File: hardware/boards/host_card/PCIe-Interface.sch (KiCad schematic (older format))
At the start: 10 parts, among them U1 ECP5UM5G-381caBGA, U7 SI5330B

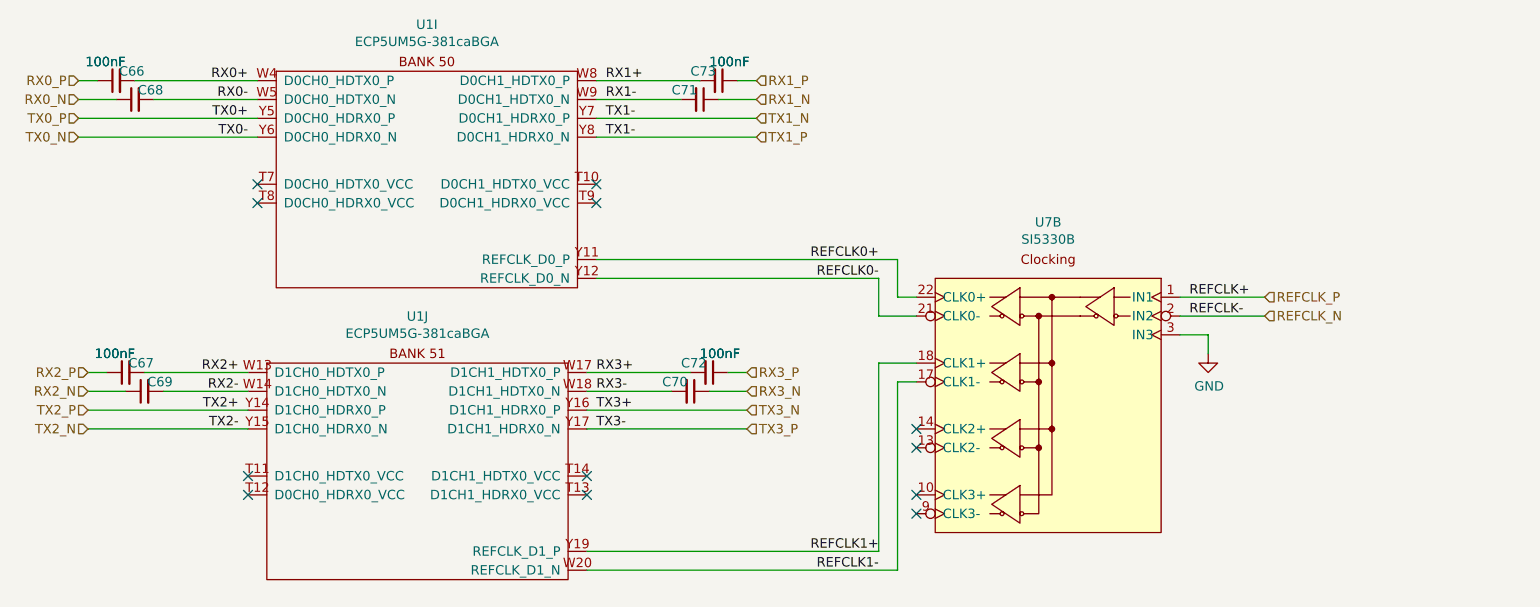
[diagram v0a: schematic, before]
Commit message: Routed the PCIe TX and RX lines + wiggles, activly routing the clock
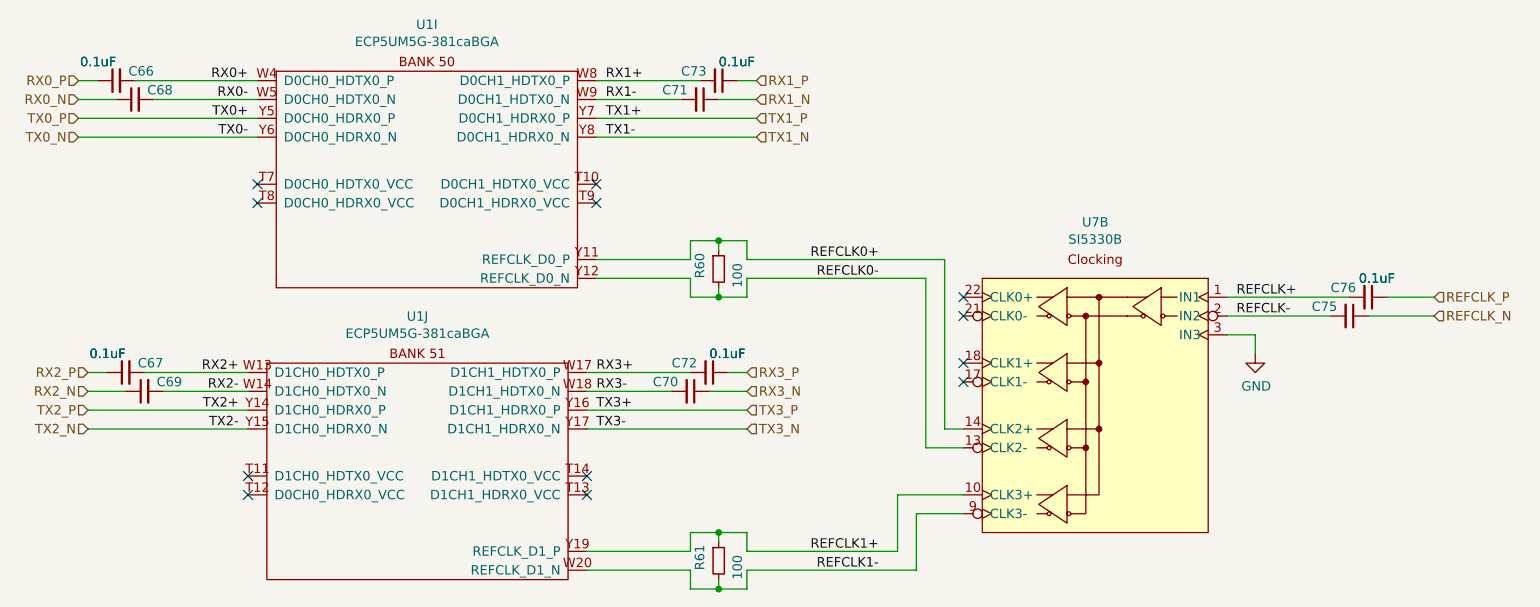
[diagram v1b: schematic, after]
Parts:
- added C75, C76: 0.1uF, Capacitor_SMD:C_0402_1005Metric, symbol Device:C_Small
- added R60, R61: 100, Resistor_SMD:R_0402_1005Metric, symbol Device:R_Small
- C66, C67, C68, C69, C70, C71, C72, C73: value 100nF -> 0.1uF
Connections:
- net REFCLK0+: now also U7.14 (CLK2+), R60.1; no longer U7.22 (CLK0+)
- net REFCLK0-: now also U7.13 (CLK2-), R60.2; no longer U7.21 (CLK0-)
- net REFCLK1+: now also U7.10 (CLK3+), R61.1; no longer U7.18 (CLK1+)
- net REFCLK1-: now also U7.9 (CLK3-), R61.2; no longer U7.17 (CLK1-)
- net REFCLK_N: now also C75.1; no longer U7.2 (IN2)
- net REFCLK_P: now also C76.1; no longer U7.1 (IN1)
- net TX1_N: no longer U1.Y7 (D0CH1_HDRX0_P)
- net TX3_N: now also U1.Y17 (D1CH1_HDRX0_N); no longer U1.Y16 (D1CH1_HDRX0_P)
- net TX3_P: now also U1.Y16 (D1CH1_HDRX0_P); no longer U1.Y17 (D1CH1_HDRX0_N)
- new net REFCLK+: C76.2, U7.1 (IN1)
- new net REFCLK-: C75.2, U7.2 (IN2)
- new net TX1_P: U1.Y7 (D0CH1_HDRX0_P)
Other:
- moved on the sheet: U7B
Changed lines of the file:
@@
 Comment4 ""
 $EndDescr
-Text HLabel 10500 3400 2    50   Input ~ 0
+Text HLabel 11400 3400 2    50   Input ~ 0
 REFCLK_P
-Text HLabel 10500 3500 2    50   Input ~ 0
+Text HLabel 11400 3500 2    50   Input ~ 0
 REFCLK_N
 Text HLabel 4200 2450 0    50   Input ~ 0
@@
 Text HLabel 4200 2550 0    50   Input ~ 0
 TX0_N
+Text HLabel 7800 2450 2    50   Input ~ 0
+TX1_P
 Text HLabel 7800 2550 2    50   Input ~ 0
-TX1_P
-Text HLabel 7800 2450 2    50   Input ~ 0
 TX1_N
 Text HLabel 4250 4000 0    50   Input ~ 0
@@
 Text HLabel 4250 4100 0    50   Input ~ 0
 TX2_N
+Text HLabel 7750 4000 2    50   Input ~ 0
+TX3_P
 Text HLabel 7750 4100 2    50   Input ~ 0
-TX3_P
-Text HLabel 7750 4000 2    50   Input ~ 0
 TX3_N
 Text HLabel 4200 2250 0    50   Input ~ 0
@@
 L lethalbit:SI5330B U7
 U 2 1 5F1A1842
-P 9350 3400
-F 0 "U7" H 9350 3798 50  0000 C CNN
-F 1 "SI5330B" H 9350 3707 50  0000 C CNN
-F 2 "Package_DFN_QFN:VQFN-24-1EP_4x4mm_P0.5mm_EP2.45x2.45mm" H 9350 3700 50  0001 C CNN
-F 3 "https://www.silabs.com/documents/public/data-sheets/Si5330.pdf" H 9350 3700 50  0001 C CNN
-F 4 "Silicon Labs" H 9350 3400 50  0001 C CNN "MFR"
-F 5 "SI5330B-B00205-GM" H 9350 3400 50  0001 C CNN "MPN"
-	2    9350 3400
+P 9600 3400
+F 0 "U7" H 9600 3798 50  0000 C CNN
+F 1 "SI5330B" H 9600 3707 50  0000 C CNN
+F 2 "Package_DFN_QFN:VQFN-24-1EP_4x4mm_P0.5mm_EP2.45x2.45mm" H 9600 3700 50  0001 C CNN
+F 3 "https://www.silabs.com/documents/public/data-sheets/Si5330.pdf" H 9600 3700 50  0001 C CNN
+F 4 "Silicon Labs" H 9600 3400 50  0001 C CNN "MFR"
+F 5 "SI5330B-B00205-GM" H 9600 3400 50  0001 C CNN "MPN"
+	2    9600 3400
 	-1   0    0    -1
 $EndComp
 Wire Wire Line
-	10050 3400 10500 3400
-Wire Wire Line
-	10050 3500 10500 3500
+	10300 3400 10950 3400
+Wire Wire Line
+	10300 3500 10850 3500
 $Comp
 L power:GND #PWR0142
 U 1 1 5F1DBF37
-P 10200 3700
-F 0 "#PWR0142" H 10200 3450 50  0001 C CNN
-F 1 "GND" H 10205 3527 50  0000 C CNN
-F 2 "" H 10200 3700 50  0001 C CNN
-F 3 "" H 10200 3700 50  0001 C CNN
-	1    10200 3700
+P 10450 3700
+F 0 "#PWR0142" H 10450 3450 50  0001 C CNN
+F 1 "GND" H 10455 3527 50  0000 C CNN
+F 2 "" H 10450 3700 50  0001 C CNN
+F 3 "" H 10450 3700 50  0001 C CNN
+	1    10450 3700
 	1    0    0    -1
 $EndComp
 Wire Wire Line
-	10050 3600 10200 3600
-Wire Wire Line
-	10200 3600 10200 3700
-NoConn ~ 8650 4100
-NoConn ~ 8650 4200
-NoConn ~ 8650 4450
-NoConn ~ 8650 4550
-Wire Wire Line
-	8650 3400 8550 3400
-Wire Wire Line
-	8550 3400 8550 3200
-Wire Wire Line
-	8550 3200 6950 3200
-Wire Wire Line
-	8650 3500 8450 3500
-Wire Wire Line
-	8450 3500 8450 3300
-Wire Wire Line
-	8450 3300 6950 3300
-Wire Wire Line
-	6900 4750 8450 4750
-Wire Wire Line
-	8450 4750 8450 3750
-Wire Wire Line
-	8450 3750 8650 3750
-Wire Wire Line
-	6900 4850 8550 4850
-Wire Wire Line
-	8550 4850 8550 3850
-Wire Wire Line
-	8550 3850 8650 3850
+	10300 3600 10450 3600
+Wire Wire Line
+	10450 3600 10450 3700
 Text Label 8450 3200 2    50   ~ 0
 REFCLK0+
@@
 AR Path="/5EF66188/5F46D592" Ref="C?"  Part="1"
 AR Path="/5ED4B101/5F46D592" Ref="C66"  Part="1"
-F 0 "C66" V 4450 2100 50  0000 L CNN
-F 1 "100nF" V 4500 2200 50  0000 L CNN
+F 0 "C66" V 4450 2050 50  0000 L CNN
+F 1 "0.1uF" V 4500 2250 50  0000 L CNN
 F 2 "Capacitor_SMD:C_0402_1005Metric" H 4400 2250 50  0001 C CNN
 F 3 "~" H 4400 2250 50  0001 C CNN
@@
 AR Path="/5EF66188/5F4C2DB2" Ref="C?"  Part="1"
 AR Path="/5ED4B101/5F4C2DB2" Ref="C68"  Part="1"
-F 0 "C68" V 4550 2200 50  0000 L CNN
-F 1 "100nF" V 4700 2400 50  0000 L CNN
+F 0 "C68" V 4550 2150 50  0000 L CNN
+F 1 "0.1uF" V 4700 2450 50  0000 L CNN
 F 2 "Capacitor_SMD:C_0402_1005Metric" H 4500 2350 50  0001 C CNN
 F 3 "~" H 4500 2350 50  0001 C CNN
@@
 AR Path="/5EF66188/5F524C27" Ref="C?"  Part="1"
 AR Path="/5ED4B101/5F524C27" Ref="C73"  Part="1"
-F 0 "C73" V 7650 2100 50  0000 L CNN
-F 1 "100nF" V 7700 2200 50  0000 L CNN
+F 0 "C73" V 7650 2050 50  0000 L CNN
+F 1 "0.1uF" V 7700 2250 50  0000 L CNN
 F 2 "Capacitor_SMD:C_0402_1005Metric" H 7600 2250 50  0001 C CNN
 F 3 "~" H 7600 2250 50  0001 C CNN
@@
 AR Path="/5EF66188/5F524C2F" Ref="C?"  Part="1"
 AR Path="/5ED4B101/5F524C2F" Ref="C71"  Part="1"
-F 0 "C71" V 7550 2200 50  0000 L CNN
-F 1 "100nF" V 7700 2400 50  0000 L CNN
+F 0 "C71" V 7550 2150 50  0000 L CNN
+F 1 "0.1uF" V 7700 2450 50  0000 L CNN
 F 2 "Capacitor_SMD:C_0402_1005Metric" H 7500 2350 50  0001 C CNN
 F 3 "~" H 7500 2350 50  0001 C CNN
@@
 AR Path="/5EF66188/5F527EEF" Ref="C?"  Part="1"
 AR Path="/5ED4B101/5F527EEF" Ref="C67"  Part="1"
-F 0 "C67" V 4500 3650 50  0000 L CNN
-F 1 "100nF" V 4550 3750 50  0000 L CNN
+F 0 "C67" V 4500 3600 50  0000 L CNN
+F 1 "0.1uF" V 4550 3800 50  0000 L CNN
 F 2 "Capacitor_SMD:C_0402_1005Metric" H 4450 3800 50  0001 C CNN
 F 3 "~" H 4450 3800 50  0001 C CNN
@@
 AR Path="/5EF66188/5F527EF7" Ref="C?"  Part="1"
 AR Path="/5ED4B101/5F527EF7" Ref="C69"  Part="1"
-F 0 "C69" V 4600 3750 50  0000 L CNN
-F 1 "100nF" V 4750 3950 50  0000 L CNN
+F 0 "C69" V 4600 3700 50  0000 L CNN
+F 1 "0.1uF" V 4750 4000 50  0000 L CNN
 F 2 "Capacitor_SMD:C_0402_1005Metric" H 4550 3900 50  0001 C CNN
 F 3 "~" H 4550 3900 50  0001 C CNN
@@
 AR Path="/5EF66188/5F52A5F2" Ref="C?"  Part="1"
 AR Path="/5ED4B101/5F52A5F2" Ref="C72"  Part="1"
-F 0 "C72" V 7600 3650 50  0000 L CNN
-F 1 "100nF" V 7650 3750 50  0000 L CNN
+F 0 "C72" V 7600 3600 50  0000 L CNN
+F 1 "0.1uF" V 7650 3800 50  0000 L CNN
 F 2 "Capacitor_SMD:C_0402_1005Metric" H 7550 3800 50  0001 C CNN
 F 3 "~" H 7550 3800 50  0001 C CNN
@@
 AR Path="/5EF66188/5F52A5FA" Ref="C?"  Part="1"
 AR Path="/5ED4B101/5F52A5FA" Ref="C70"  Part="1"
-F 0 "C70" V 7500 3750 50  0000 L CNN
-F 1 "100nF" V 7650 3950 50  0000 L CNN
+F 0 "C70" V 7500 3700 50  0000 L CNN
+F 1 "0.1uF" V 7650 4000 50  0000 L CNN
 F 2 "Capacitor_SMD:C_0402_1005Metric" H 7450 3900 50  0001 C CNN
 F 3 "~" H 7450 3900 50  0001 C CNN
@@
 Text Label 7000 2350 0    50   ~ 0
 RX1-
-Text Label 7000 2450 0    50   ~ 0
-TX1-
 Text Label 7000 2550 0    50   ~ 0
 TX1-
-Text Label 10100 3400 0    50   ~ 0
+Text Label 7000 2450 0    50   ~ 0
+TX1+
+Text Label 10350 3400 0    50   ~ 0
 REFCLK+
-Text Label 10100 3500 0    50   ~ 0
+Text Label 10350 3500 0    50   ~ 0
 REFCLK-
+$Comp
+L Device:R_Small R?
+U 1 1 5F0E60AE
+P 7600 3250
+AR Path="/5EDAB834/5F0E60AE" Ref="R?"  Part="1"
+AR Path="/5EF6A128/5F0E60AE" Ref="R?"  Part="1"
+AR Path="/5ED4B101/5F0E60AE" Ref="R60"  Part="1"
+F 0 "R60" V 7500 3200 50  0000 L CNN
+F 1 "100" V 7700 3150 50  0000 L CNN
+F 2 "Resistor_SMD:R_0402_1005Metric" H 7600 3250 50  0001 C CNN
+F 3 "~" H 7600 3250 50  0001 C CNN
+F 4 "Vishay Dale" H 7600 3250 50  0001 C CNN "MFR"
+F 5 "RCS0402100RFKED" V 7600 3250 50  0001 C CNN "MPN"
+	1    7600 3250
+	1    0    0    -1
+$EndComp
+$Comp
+L Device:R_Small R?
+U 1 1 5F0E8C33
+P 7600 4800
+AR Path="/5EDAB834/5F0E8C33" Ref="R?"  Part="1"
+AR Path="/5EF6A128/5F0E8C33" Ref="R?"  Part="1"
+AR Path="/5ED4B101/5F0E8C33" Ref="R61"  Part="1"
+F 0 "R61" V 7500 4750 50  0000 L CNN
+F 1 "100" V 7700 4700 50  0000 L CNN
+F 2 "Resistor_SMD:R_0402_1005Metric" H 7600 4800 50  0001 C CNN
+F 3 "~" H 7600 4800 50  0001 C CNN
+F 4 "Vishay Dale" H 7600 4800 50  0001 C CNN "MFR"
+F 5 "RCS0402100RFKED" V 7600 4800 50  0001 C CNN "MPN"
+	1    7600 4800
+	1    0    0    -1
+$EndComp
+Wire Wire Line
+	7750 4850 7750 4950
+Wire Wire Line
+	7750 4950 7600 4950
+Wire Wire Line
+	7450 4950 7450 4850
+Wire Wire Line
+	7450 4850 6900 4850
+Wire Wire Line
+	6900 4750 7450 4750
+Wire Wire Line
+	7450 4750 7450 4650
+Wire Wire Line
+	7450 4650 7600 4650
+Wire Wire Line
+	7750 4650 7750 4750
+Wire Wire Line
+	7600 4700 7600 4650
+Connection ~ 7600 4650
+Wire Wire Line
+	7600 4650 7750 4650
+Wire Wire Line
+	7600 4900 7600 4950
+Connection ~ 7600 4950
+Wire Wire Line
+	7600 4950 7450 4950
+Wire Wire Line
+	7750 3300 7750 3400
+Wire Wire Line
+	7750 3400 7600 3400
+Wire Wire Line
+	7450 3400 7450 3300
+Wire Wire Line
+	7450 3300 6950 3300
+Wire Wire Line
+	6950 3200 7450 3200
+Wire Wire Line
+	7450 3200 7450 3100
+Wire Wire Line
+	7450 3100 7600 3100
+Wire Wire Line
+	7750 3100 7750 3200
+Wire Wire Line
+	7600 3150 7600 3100
+Connection ~ 7600 3100
+Wire Wire Line
+	7600 3100 7750 3100
+Wire Wire Line
+	7600 3400 7600 3350
+Connection ~ 7600 3400
+Wire Wire Line
+	7600 3400 7450 3400
+Wire Wire Line
+	8700 3300 8700 4200
+Wire Wire Line
+	7750 3300 8700 3300
+Wire Wire Line
+	8800 3200 8800 4100
+Wire Wire Line
+	7750 3200 8800 3200
+Wire Wire Line
+	8550 4750 8550 4450
+Wire Wire Line
+	7750 4750 8550 4750
+Wire Wire Line
+	8650 4850 8650 4550
+Wire Wire Line
+	7750 4850 8650 4850
+NoConn ~ 8900 3400
+NoConn ~ 8900 3500
+NoConn ~ 8900 3750
+NoConn ~ 8900 3850
+Wire Wire Line
+	8700 4200 8900 4200
+Wire Wire Line
+	8800 4100 8900 4100
+Wire Wire Line
+	8550 4450 8900 4450
+Wire Wire Line
+	8650 4550 8900 4550
+$Comp
+L Device:C_Small C?
+U 1 1 5F1F0713
+P 11050 3400
+AR Path="/5EF66188/5F1F0713" Ref="C?"  Part="1"
+AR Path="/5ED4B101/5F1F0713" Ref="C76"  Part="1"
+F 0 "C76" V 11100 3200 50  0000 L CNN
+F 1 "0.1uF" V 11150 3350 50  0000 L CNN
+F 2 "Capacitor_SMD:C_0402_1005Metric" H 11050 3400 50  0001 C CNN
+F 3 "~" H 11050 3400 50  0001 C CNN
+F 4 "KEMET" H 11050 3400 50  0001 C CNN "MFR"
+F 5 "C0402C104M8PACTU" H 11050 3400 50  0001 C CNN "MPN"
+	1    11050 3400
+	0    1    -1   0
+$EndComp
+Wire Wire Line
+	11150 3400 11400 3400
+Wire Wire Line
+	11050 3500 11400 3500
+$Comp
+L Device:C_Small C?
+U 1 1 5F217313
+P 10950 3500
+AR Path="/5EF66188/5F217313" Ref="C?"  Part="1"
+AR Path="/5ED4B101/5F217313" Ref="C75"  Part="1"
+F 0 "C75" V 11000 3300 50  0000 L CNN
+F 1 "0.1uF" V 11150 3550 50  0000 L CNN
+F 2 "Capacitor_SMD:C_0402_1005Metric" H 10950 3500 50  0001 C CNN
+F 3 "~" H 10950 3500 50  0001 C CNN
+F 4 "KEMET" H 10950 3500 50  0001 C CNN "MFR"
+F 5 "C0402C104M8PACTU" H 10950 3500 50  0001 C CNN "MPN"
+	1    10950 3500
+	0    1    -1   0
+$EndComp
 $EndSCHEMATC

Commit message: Fixed  / updated the ECP5 symbol for the ECP5UM5G-85K
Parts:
- U1: symbol lethalbit:ECP5UM5G-381caBGA -> lethalbit:LFE5UM5G-85F-8BG381I
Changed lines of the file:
@@
 	4600 2350 5150 2350
 $Comp
-L lethalbit:ECP5UM5G-381caBGA U1
+L lethalbit:LFE5UM5G-85F-8BG381I U1
 U 9 1 5F0889A2
 P 6050 2300
+AR Path="/5F0889A2" Ref="U1"  Part="9"
+AR Path="/5ED4B101/5F0889A2" Ref="U1"  Part="9"
 F 0 "U1" H 6050 2648 50  0000 C CNN
 F 1 "ECP5UM5G-381caBGA" H 6050 2557 50  0000 C CNN
@@
 $EndComp
 $Comp
-L lethalbit:ECP5UM5G-381caBGA U1
+L lethalbit:LFE5UM5G-85F-8BG381I U1
 U 10 1 5F0889A8
 P 6000 3850
+AR Path="/5F0889A8" Ref="U1"  Part="10"
+AR Path="/5ED4B101/5F0889A8" Ref="U1"  Part="10"
 F 0 "U1" H 6000 4198 50  0000 C CNN
 F 1 "ECP5UM5G-381caBGA" H 6000 4107 50  0000 C CNN
